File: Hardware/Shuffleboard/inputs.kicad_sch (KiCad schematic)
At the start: 16 parts, among them U1 COM-09032

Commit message: led's, mux
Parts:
- added D1: Red, LED_THT:LED_D5.0mm, symbol Device:LED
- added IC1: DG3157EDL-T1-GE3, SOT65P210X110-6N, symbol MuxShuff:DG3157EDL-T1-GE3
- added R10: 500, Resistor_SMD:R_0603_1608Metric_Pad0.98x0.95mm_HandSolder, symbol Device:R
- added R12, R45, R9: 10k, Resistor_SMD:R_0603_1608Metric_Pad0.98x0.95mm_HandSolder, symbol Device:R
- added U3: LMV331, symbol Comparator:LMV331
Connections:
- net +3.3V: now also IC1.5 (V+), R12.1, R45.1, U3.5 (V+)
- net GND: now also D1.1 (K), IC1.2 (GND), R9.2, U3.2 (V-)
- net VER_PB19_ADC1_6: now also IC1.4 (A); no longer C5.1, R4.2
- new net: D1.2 (A), R10.2
- new net CompOut: IC1.6 (S), R10.1, R12.2, U3.4
- new net VER_POT: C5.1, IC1.3 (B0), R4.2, U3.3 (-)
- new net Vref: IC1.1 (B1), R45.2, R9.1, U3.1 (+)
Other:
- note added: "ADC Output is GND if joystick is moved downwards"
- note added: "Comparator/Output Circuit"

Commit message: fixed inverting input
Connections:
- net VER_POT: now also U3.1 (+); no longer U3.3 (-)
- net Vref: now also U3.3 (-); no longer U3.1 (+)
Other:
- moved on the sheet: R45, R9
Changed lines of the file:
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@@
 	)
 	(junction
-		(at 203.2 34.29)
+		(at 203.2 39.37)
 		(diameter 0)
 		(color 0 0 0 0)
@@
 	(wire
 		(pts
-			(xy 203.2 33.02) (xy 203.2 34.29)
+			(xy 203.2 38.1) (xy 203.2 39.37)
 		)
 		(stroke
@@
 	(wire
 		(pts
-			(xy 203.2 34.29) (xy 203.2 36.83)
+			(xy 203.2 39.37) (xy 203.2 41.91)
 		)
 		(stroke
@@
 	(wire
 		(pts
-			(xy 203.2 34.29) (xy 214.63 34.29)
+			(xy 203.2 39.37) (xy 214.63 39.37)
 		)
 		(stroke
@@
 	)
 	(label "VER_POT"
+		(at 214.63 34.29 180)
+		(effects
+			(font
+				(size 1.27 1.27)
+				(thickness 0.1588)
+			)
+			(justify right bottom)
+		)
+	)
+	(label "VER_POT"
 		(at 168.91 58.42 0)
 		(effects
@@
 	)
 	(label "Vref"
-		(at 203.2 34.29 180)
+		(at 203.2 39.37 180)
 		(effects
 			(font
@@
 		)
 	)
-	(label "VER_POT"
-		(at 214.63 39.37 180)
-		(effects
-			(font
-				(size 1.27 1.27)
-				(thickness 0.1588)
-			)
-			(justify right bottom)
-		)
-	)
 	(hierarchical_label "VER_PB19_ADC1_6"
 		(shape output)
@@
 	(symbol
 		(lib_id "power:+3.3V")
-		(at 203.2 25.4 0)
+		(at 203.2 30.48 0)
 		(unit 1)
 		(exclude_from_sim no)
@@
 		(fields_autoplaced yes)
 		(property "Reference" "#PWR026"
-			(at 203.2 29.21 0)
+			(at 203.2 34.29 0)
 			(effects
 				(font
@@
 		)
 		(property "Value" "+3.3V"
-			(at 203.2001 21.59 90)
+			(at 203.2001 26.67 90)
 			(effects
 				(font
@@
 		)
 		(property "Footprint" ""
-			(at 203.2 25.4 0)
+			(at 203.2 30.48 0)
 			(effects
 				(font
@@
 		)
 		(property "Datasheet" ""
-			(at 203.2 25.4 0)
+			(at 203.2 30.48 0)
 			(effects
 				(font
@@
 		)
 		(property "Description" "Power symbol creates a global label with name \"+3.3V\""
-			(at 203.2 25.4 0)
+			(at 203.2 30.48 0)
 			(effects
 				(font
@@
 	(symbol
 		(lib_id "power:GND")
-		(at 203.2 44.45 0)
+		(at 203.2 49.53 0)
 		(unit 1)
 		(exclude_from_sim no)
@@
 		(fields_autoplaced yes)
 		(property "Reference" "#PWR027"
-			(at 203.2 50.8 0)
+			(at 203.2 55.88 0)
 			(effects
 				(font
@@
 		)
 		(property "Value" "GND"
-			(at 203.2001 48.26 90)
+			(at 203.2001 53.34 90)
 			(effects
 				(font
@@
 		)
 		(property "Footprint" ""
-			(at 203.2 44.45 0)
+			(at 203.2 49.53 0)
 			(effects
 				(font
@@
 		)
 		(property "Datasheet" ""
-			(at 203.2 44.45 0)
+			(at 203.2 49.53 0)
 			(effects
 				(font
@@
 		)
 		(property "Description" "Power symbol creates a global label with name \"GND\" , ground"
-			(at 203.2 44.45 0)
+			(at 203.2 49.53 0)
 			(effects
 				(font
@@
 	(symbol
 		(lib_id "Device:R")
-		(at 203.2 40.64 0)
+		(at 203.2 45.72 0)
 		(unit 1)
 		(exclude_from_sim no)
@@
 		(dnp no)
 		(property "Reference" "R9"
-			(at 200.66 40.386 90)
+			(at 200.66 45.466 90)
 			(effects
 				(font
@@
 		)
 		(property "Value" "10k"
-			(at 198.12 40.386 90)
+			(at 198.12 45.466 90)
 			(effects
 				(font
@@
 		)
 		(property "Footprint" "Resistor_SMD:R_0603_1608Metric_Pad0.98x0.95mm_HandSolder"
-			(at 201.422 40.64 90)
+			(at 201.422 45.72 90)
 			(effects
 				(font
@@
 		)
 		(property "Datasheet" "~"
-			(at 203.2 40.64 0)
+			(at 203.2 45.72 0)
 			(effects
 				(font
@@
 		)
 		(property "Description" "Resistor"
-			(at 203.2 40.64 0)
+			(at 203.2 45.72 0)
 			(effects
 				(font
@@
 		)
 		(property "Mouser Link" "https://www.mouser.com/ProductDetail/Vishay/CRCW060310K0FKEA?qs=pAO1Z172M84BVnhDjtnsoQ%3D%3D"
-			(at 203.2 40.64 0)
+			(at 203.2 45.72 0)
 			(effects
 				(font
@@
 		)
 		(property "JLCPCB #" "C25804"
-			(at 203.2 40.64 0)
+			(at 203.2 45.72 0)
 			(effects
 				(font
@@
 		)
 		(property "Mouser Part Number" "71-CRCW0603-10K-E3"
-			(at 203.2 40.64 0)
+			(at 203.2 45.72 0)
 			(effects
 				(font
@@
 	(symbol
 		(lib_id "Device:R")
-		(at 203.2 29.21 0)
+		(at 203.2 34.29 0)
 		(unit 1)
 		(exclude_from_sim no)
@@
 		(dnp no)
 		(property "Reference" "R45"
-			(at 200.66 28.956 90)
+			(at 200.66 34.036 90)
 			(effects
 				(font
@@
 		)
 		(property "Value" "10k"
-			(at 198.12 28.956 90)
+			(at 198.12 34.036 90)
 			(effects
 				(font
@@
 		)
 		(property "Footprint" "Resistor_SMD:R_0603_1608Metric_Pad0.98x0.95mm_HandSolder"
-			(at 201.422 29.21 90)
+			(at 201.422 34.29 90)
 			(effects
 				(font
@@
 		)
 		(property "Datasheet" "~"
-			(at 203.2 29.21 0)
+			(at 203.2 34.29 0)
 			(effects
 				(font
@@
 		)
 		(property "Description" "Resistor"
-			(at 203.2 29.21 0)
+			(at 203.2 34.29 0)
 			(effects
 				(font
@@
 		)
 		(property "Mouser Link" "https://www.mouser.com/ProductDetail/Vishay/CRCW060310K0FKEA?qs=pAO1Z172M84BVnhDjtnsoQ%3D%3D"
-			(at 203.2 29.21 0)
+			(at 203.2 34.29 0)
 			(effects
 				(font
@@
 		)
 		(property "JLCPCB #" "C25804"
-			(at 203.2 29.21 0)
+			(at 203.2 34.29 0)
 			(effects
 				(font
@@
 		)
 		(property "Mouser Part Number" "71-CRCW0603-10K-E3"
-			(at 203.2 29.21 0)
+			(at 203.2 34.29 0)
 			(effects
 				(font

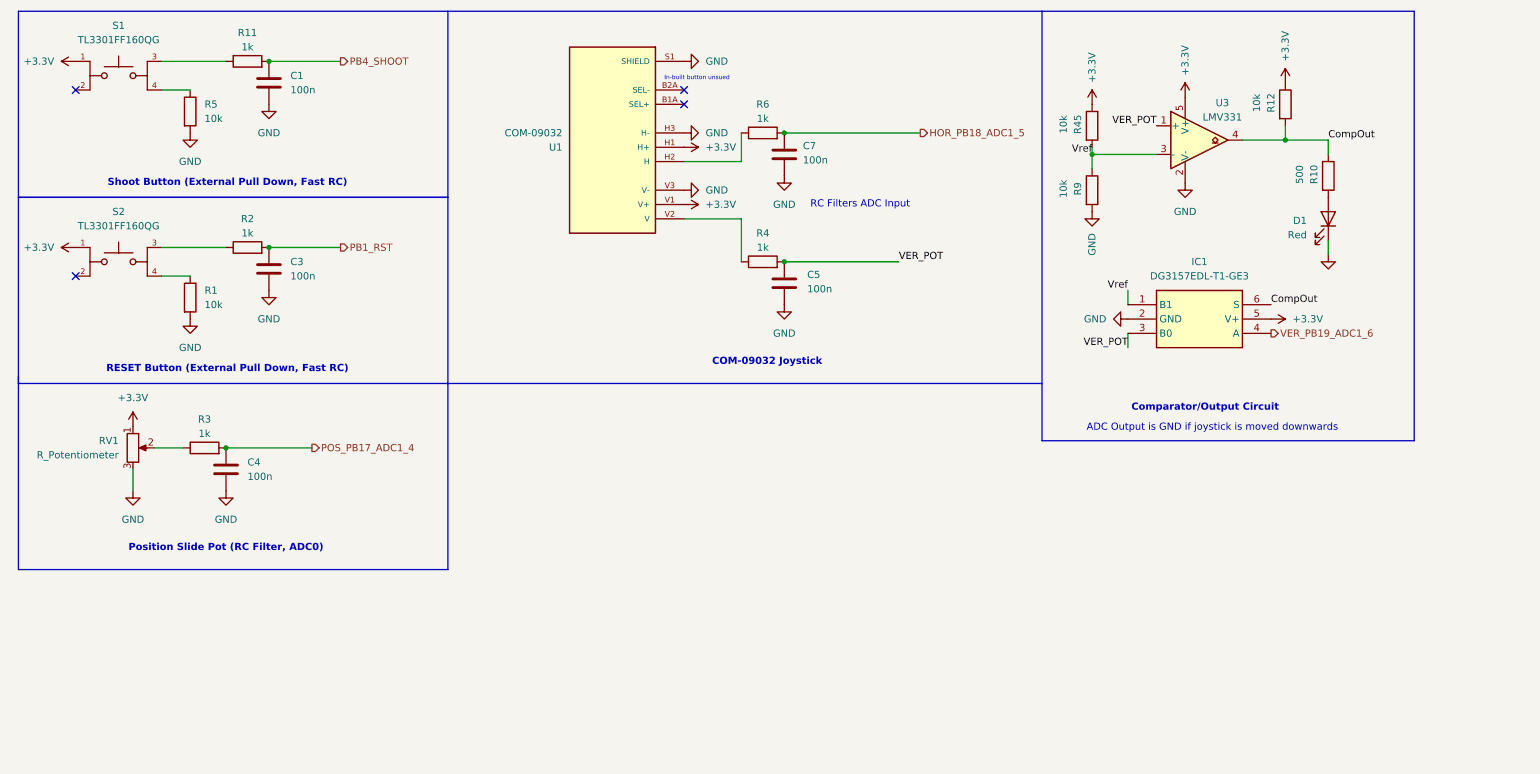
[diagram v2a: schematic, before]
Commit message: invalid button handling
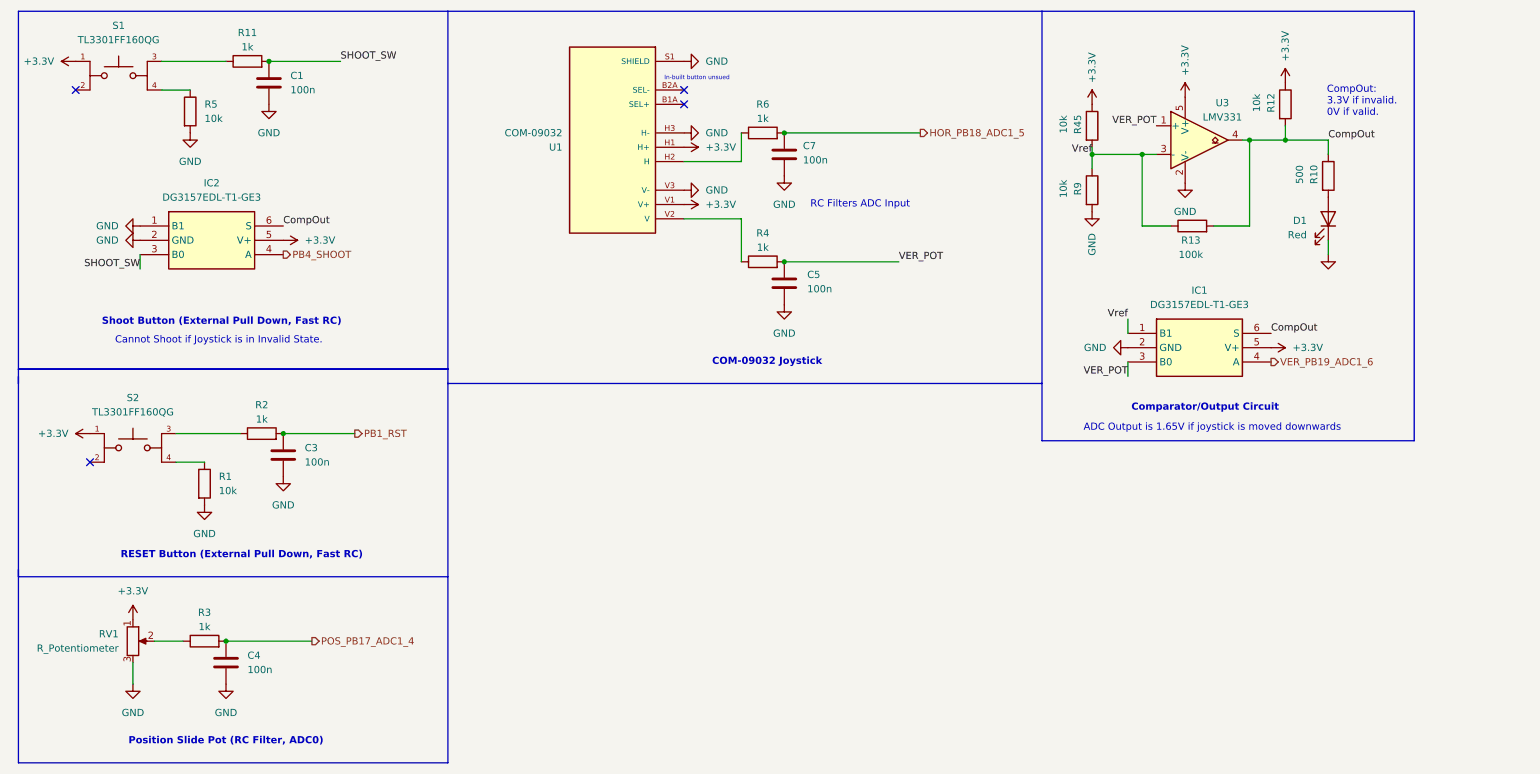
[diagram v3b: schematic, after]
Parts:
- added IC2: DG3157EDL-T1-GE3, SOT65P210X110-6N, symbol MuxShuff:DG3157EDL-T1-GE3
- added R13: 100k, Resistor_SMD:R_0603_1608Metric_Pad0.98x0.95mm_HandSolder, symbol Device:R
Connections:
- net +3.3V: now also IC2.5 (V+)
- net CompOut: now also IC2.6 (S), R13.2
- net GND: now also IC2.1 (B1), IC2.2 (GND)
- net PB4_SHOOT: now also IC2.4 (A); no longer C1.1, R11.2
- net Vref: now also R13.1
- new net SHOOT_SW: C1.1, IC2.3 (B0), R11.2
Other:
- note added: "ADC Output is 1.65V if joystick is moved downwards"
- note added: "Cannot Shoot if Joystick is in Invalid State."
- note added: "CompOut: 3.3V if invalid. 0V if valid."
- note removed: "ADC Output is GND if joystick is moved downwards"
- moved on the sheet: C3, C4, IC1, R1, R2, R3, RV1, S2

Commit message: fet led driving
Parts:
- added Q1: NMOS, ShuffleboardFootprints:SOT95P260X110-3N, symbol Simulation_SPICE:NMOS
- IC1, IC2: footprint SOT65P210X110-6N -> ShuffleboardFootprints:SOT65P210X110-6N; Mouser Link (none) -> google.com/search?q=78-DG3157EDL-T1-GE3&oq=78-DG3157EDL-T1-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
- U3: footprint (none) -> ShuffleboardFootprints:lmv331
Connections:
- net +3.3V: now also D1.2 (A)
- net CompOut: now also Q1.2 (G); no longer R10.1
- net GND: now also Q1.3 (S); no longer D1.1 (K)
- net at R10.2: now also Q1.1 (D); no longer D1.2 (A)
- new net: D1.1 (K), R10.1
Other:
- moved on the sheet: D1, R10

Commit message: led driving fet
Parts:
- R10: value 500 -> 330; footprint Resistor_SMD:R_0603_1608Metric_Pad0.98x0.95mm_HandSolder -> Resistor_SMD:R_2010_5025Metric_Pad1.40x2.65mm_HandSolder; Mouser Link https://www.mouser.com/ProductDetail/YAGEO/RE0603DRE07511RL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 -> https://www.mouser.com/ProductDetail/TE-Connectivity-Holswo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; Mouser Part Number 603-RE0603DRE07511RL -> 279-CRGCQ2010F330R
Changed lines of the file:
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@@
 			)
 		)
-		(property "Value" "500"
+		(property "Value" "330"
 			(at 246.38 27.686 90)
 			(effects
@@
 			)
 		)
-		(property "Footprint" "Resistor_SMD:R_0603_1608Metric_Pad0.98x0.95mm_HandSolder"
+		(property "Footprint" "Resistor_SMD:R_2010_5025Metric_Pad1.40x2.65mm_HandSolder"
 			(at 249.682 27.94 90)
 			(effects
@@
 			)
 		)
-		(property "Mouser Link" "https://www.mouser.com/ProductDetail/YAGEO/RE0603DRE07511RL?qs=k2KEx2DUIRRHZePwM2PQsA%3D%3D"
+		(property "Mouser Link" "https://www.mouser.com/ProductDetail/TE-Connectivity-Holsworthy/CRGCQ2010F330R?qs=wUXugUrL1qwW9IDGKnwDXA%3D%3D"
 			(at 251.46 27.94 0)
 			(effects
@@
 			)
 		)
-		(property "Mouser Part Number" "603-RE0603DRE07511RL"
+		(property "Mouser Part Number" "279-CRGCQ2010F330R"
 			(at 251.46 27.94 0)
 			(effects

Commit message: series gate resistor
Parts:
- added R14: 330, Resistor_SMD:R_2010_5025Metric_Pad1.40x2.65mm_HandSolder, symbol Device:R
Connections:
- net CompOut: now also R14.2; no longer Q1.2 (G)
- new net: Q1.2 (G), R14.1
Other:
- moved on the sheet: D1, Q1, R10
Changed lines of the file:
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@@
 	(wire
 		(pts
-			(xy 237.49 36.83) (xy 243.84 36.83)
+			(xy 237.49 36.83) (xy 245.11 36.83)
 		)
 		(stroke
@@
 	(polyline
 		(pts
-			(xy 271.78 13.97) (xy 194.31 13.97)
+			(xy 280.67 13.97) (xy 194.31 13.97)
 		)
 		(stroke
@@
 	(polyline
 		(pts
-			(xy 194.31 90.17) (xy 271.78 90.17)
+			(xy 194.31 90.17) (xy 280.67 90.17)
 		)
 		(stroke
@@
 	(polyline
 		(pts
-			(xy 271.78 90.17) (xy 271.78 13.97)
+			(xy 280.67 90.17) (xy 280.67 13.97)
 		)
 		(stroke
@@
 	(symbol
 		(lib_id "power:+3.3V")
-		(at 259.08 24.13 270)
+		(at 267.97 24.13 270)
 		(unit 1)
 		(exclude_from_sim no)
@@
 		(fields_autoplaced yes)
 		(property "Reference" "#PWR032"
-			(at 255.27 24.13 0)
+			(at 264.16 24.13 0)
 			(effects
 				(font
@@
 		)
 		(property "Value" "+3.3V"
-			(at 262.89 24.1299 90)
+			(at 271.78 24.1299 90)
 			(effects
 				(font
@@
 		)
 		(property "Footprint" ""
-			(at 259.08 24.13 0)
+			(at 267.97 24.13 0)
 			(effects
 				(font
@@
 		)
 		(property "Datasheet" ""
-			(at 259.08 24.13 0)
+			(at 267.97 24.13 0)
 			(effects
 				(font
@@
 		)
 		(property "Description" "Power symbol creates a global label with name \"+3.3V\""
-			(at 259.08 24.13 0)
+			(at 267.97 24.13 0)
 			(effects
 				(font
@@
 	(symbol
 		(lib_id "power:GND")
-		(at 251.46 41.91 0)
+		(at 260.35 41.91 0)
 		(unit 1)
 		(exclude_from_sim no)
@@
 		(fields_autoplaced yes)
 		(property "Reference" "#PWR037"
-			(at 251.46 48.26 0)
+			(at 260.35 48.26 0)
 			(effects
 				(font
@@
 		)
 		(property "Value" "GND"
-			(at 251.46 46.99 0)
+			(at 260.35 46.99 0)
 			(effects
 				(font
@@
 		)
 		(property "Footprint" ""
-			(at 251.46 41.91 0)
+			(at 260.35 41.91 0)
 			(effects
 				(font
@@
 		)
 		(property "Datasheet" ""
-			(at 251.46 41.91 0)
+			(at 260.35 41.91 0)
 			(effects
 				(font
@@
 		)
 		(property "Description" "Power symbol creates a global label with name \"GND\" , ground"
-			(at 251.46 41.91 0)
+			(at 260.35 41.91 0)
 			(effects
 				(font
@@
 	(symbol
 		(lib_id "Device:LED")
-		(at 255.27 24.13 0)
+		(at 264.16 24.13 0)
 		(mirror x)
 		(unit 1)
@@
 		(dnp no)
 		(property "Reference" "D1"
-			(at 254.9526 20.32 90)
+			(at 263.8426 20.32 90)
 			(effects
 				(font
@@
 		)
 		(property "Value" "Red"
-			(at 252.4126 20.32 90)
+			(at 261.3026 20.32 90)
 			(effects
 				(font
@@
 		)
 		(property "Footprint" "LED_THT:LED_D5.0mm"
-			(at 255.27 24.13 0)
+			(at 264.16 24.13 0)
 			(effects
 				(font
@@
 		)
 		(property "Datasheet" "https://www.mouser.com/datasheet/3/350/1/C18734.pdf"
-			(at 255.27 24.13 0)
+			(at 264.16 24.13 0)
 			(effects
 				(font
@@
 		)
 		(property "Description" "Light emitting diode"
-			(at 255.27 24.13 0)
+			(at 264.16 24.13 0)
 			(effects
 				(font
@@
 		)
 		(property "Mouser Link" "https://www.mouser.com/ProductDetail/Dialight/521-8714F?qs=VVKQmw408U8Hoj3%252BT2bJjA%3D%3D"
-			(at 255.27 24.13 90)
+			(at 264.16 24.13 90)
 			(effects
 				(font
@@
 		)
 		(property "JLCPCB #" ""
-			(at 255.27 24.13 0)
+			(at 264.16 24.13 0)
 			(effects
 				(font
@@
 		)
 		(property "Mouser Part Number" "645-521-8714F"
-			(at 255.27 24.13 90)
+			(at 264.16 24.13 90)
 			(effects
 				(font
@@
 	)
 	(symbol
+		(lib_id "Device:R")
+		(at 248.92 36.83 270)
+		(unit 1)
+		(exclude_from_sim no)
+		(in_bom yes)
+		(on_board yes)
+		(dnp no)
+		(property "Reference" "R14"
+			(at 249.174 34.29 90)
+			(effects
+				(font
+					(size 1.27 1.27)
+				)
+			)
+		)
+		(property "Value" "330"
+			(at 249.174 31.75 90)
+			(effects
+				(font
+					(size 1.27 1.27)
+				)
+			)
+		)
+		(property "Footprint" "Resistor_SMD:R_2010_5025Metric_Pad1.40x2.65mm_HandSolder"
+			(at 248.92 35.052 90)
+			(effects
+				(font
+					(size 1.27 1.27)
+				)
+				(hide yes)
+			)
+		)
+		(property "Datasheet" "~"
+			(at 248.92 36.83 0)
+			(effects
+				(font
+					(size 1.27 1.27)
+				)
+				(hide yes)
+			)
+		)
+		(property "Description" "Resistor"
+			(at 248.92 36.83 0)
+			(effects
+				(font
+					(size 1.27 1.27)
+				)
+				(hide yes)
+			)
+		)
+		(property "Mouser Link" "https://www.mouser.com/ProductDetail/TE-Connectivity-Holsworthy/CRGCQ2010F330R?qs=wUXugUrL1qwW9IDGKnwDXA%3D%3D"
+			(at 248.92 36.83 0)
+			(effects
+				(font
+					(size 1.27 1.27)
+				)
+				(hide yes)
+			)
+		)
+		(property "JLCPCB #" ""
+			(at 248.92 36.83 0)
+			(effects
+				(font
+					(size 1.27 1.27)
+				)
+				(hide yes)
+			)
+		)
+		(property "Mouser Part Number" "279-CRGCQ2010F330R"
+			(at 248.92 36.83 0)
+			(effects
+				(font
+					(size 1.27 1.27)
+				)
+				(hide yes)
+			)
+		)
+		(pin "2"
+		)
+		(pin "1"
+		)
+		(instances
+			(project "Shuffleboard"
+				(path "/8d05e546-da1a-40d0-9e47-08c4b800bb0e/64806a61-d157-4b9f-a3a2-54f9af1ae5be"
+					(reference "R14")
+					(unit 1)
+				)
+			)
+		)
+	)
+	(symbol
 		(lib_id "power:+3.3V")
 		(at 237.49 26.67 0)
@@
 	(symbol
 		(lib_id "Simulation_SPICE:NMOS")
-		(at 248.92 36.83 0)
+		(at 257.81 36.83 0)
 		(unit 1)
 		(exclude_from_sim no)
@@
 		(fields_autoplaced yes)
 		(property "Reference" "Q1"
-			(at 255.27 35.5599 0)
+			(at 264.16 35.5599 0)
 			(effects
 				(font
@@
 		)
 		(property "Value" "NMOS"
-			(at 255.27 38.0999 0)
+			(at 264.16 38.0999 0)
 			(effects
 				(font
@@
 		)
 		(property "Footprint" "ShuffleboardFootprints:SOT95P260X110-3N"
-			(at 254 34.29 0)
+			(at 262.89 34.29 0)
 			(effects
 				(font
@@
 		)
 		(property "Datasheet" "https://ngspice.sourceforge.io/docs/ngspice-html-manual/manual.xhtml#cha_MOSFETs"
-			(at 248.92 49.53 0)
+			(at 257.81 49.53 0)
 			(effects
 				(font
@@
 		)
 		(property "Description" "N-MOSFET transistor, drain/source/gate"
-			(at 248.92 36.83 0)
+			(at 257.81 36.83 0)
 			(effects
 				(font
@@
 		)
 		(property "Sim.Device" "NMOS"
-			(at 248.92 53.975 0)
+			(at 257.81 53.975 0)
 			(effects
 				(font
@@
 		)
 		(property "Sim.Type" "VDMOS"
-			(at 248.92 55.88 0)
+			(at 257.81 55.88 0)
 			(effects
 				(font
@@
 		)
 		(property "Sim.Pins" "1=D 2=G 3=S"
-			(at 248.92 52.07 0)
+			(at 257.81 52.07 0)
 			(effects
 				(font
@@
 		)
 		(property "Mouser Link" "https://www.mouser.com/ProductDetail/Infineon-Technologies/2N7002-H6327?qs=CVg1V728NXGZyf6kD1tkzQ%3D%3D"
-			(at 248.92 36.83 0)
+			(at 257.81 36.83 0)
 			(effects
 				(font
@@
 		)
 		(property "Mouser Part Number" "726-2N7002H6327"
-			(at 248.92 36.83 0)
+			(at 257.81 36.83 0)
 			(effects
 				(font
@@
 	(symbol
 		(lib_id "Device:R")
-		(at 251.46 27.94 0)
+		(at 260.35 27.94 0)
 		(unit 1)
 		(exclude_from_sim no)
@@
 		(dnp no)
 		(property "Reference" "R10"
-			(at 248.92 27.686 90)
+			(at 257.81 27.686 90)
 			(effects
 				(font
@@
 		)
 		(property "Value" "330"
-			(at 246.38 27.686 90)
+			(at 255.27 27.686 90)
 			(effects
 				(font
@@
 		)
 		(property "Footprint" "Resistor_SMD:R_2010_5025Metric_Pad1.40x2.65mm_HandSolder"
-			(at 249.682 27.94 90)
+			(at 258.572 27.94 90)
 			(effects
 				(font
@@
 		)
 		(property "Datasheet" "~"
-			(at 251.46 27.94 0)
+			(at 260.35 27.94 0)
 			(effects
 				(font
@@
 		)
 		(property "Description" "Resistor"
-			(at 251.46 27.94 0)
+			(at 260.35 27.94 0)
 			(effects
 				(font
@@
 		)
 		(property "Mouser Link" "https://www.mouser.com/ProductDetail/TE-Connectivity-Holsworthy/CRGCQ2010F330R?qs=wUXugUrL1qwW9IDGKnwDXA%3D%3D"
-			(at 251.46 27.94 0)
+			(at 260.35 27.94 0)
 			(effects
 				(font
@@
 		)
 		(property "JLCPCB #" ""
-			(at 251.46 27.94 0)
+			(at 260.35 27.94 0)
 			(effects
 				(font
@@
 		)
 		(property "Mouser Part Number" "279-CRGCQ2010F330R"
-			(at 251.46 27.94 0)
+			(at 260.35 27.94 0)
 			(effects
 				(font

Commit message: finished layout
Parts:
- C1, C3, C4, C5, C7: value 100n -> (none)
- D1: value Red -> (none)
- IC1, IC2: value DG3157EDL-T1-GE3 -> (none)
- Q1: value NMOS -> (none)
- R1, R12, R45, R5, R9: value 10k -> (none); footprint Resistor_SMD:R_0603_1608Metric_Pad0.98x0.95mm_HandSolder -> Resistor_THT:R_Axial_DIN0207_L6.3mm_D2.5mm_P7.62mm_Horizontal
- R10, R14: value 330 -> (none)
- R11, R2, R3, R4, R6: value 1k -> (none); footprint Resistor_SMD:R_0603_1608Metric_Pad0.98x0.95mm_HandSolder -> Resistor_THT:R_Axial_DIN0207_L6.3mm_D2.5mm_P7.62mm_Horizontal
- R13: value 100k -> (none)
- RV1: value R_Potentiometer -> (none)
- S1, S2: value TL3301FF160QG -> (none)
- U1: value COM-09032 -> (none)
- U3: value LMV331 -> (none)
